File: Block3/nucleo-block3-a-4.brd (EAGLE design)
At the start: 100.3 x 80 mm, 91 parts, among them IC2 TL331, J4 MODJACK6P6C-MJ3245-66-0CONN_M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, J5 MODJACK6P6C-MJ3245-66-0CONN_M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, Q1 NPN-23, Q3 BSS84, Q4 BSS123, U1 TC4428ACOA, U2 TC4428ACOA, U3 TC4428ACOA

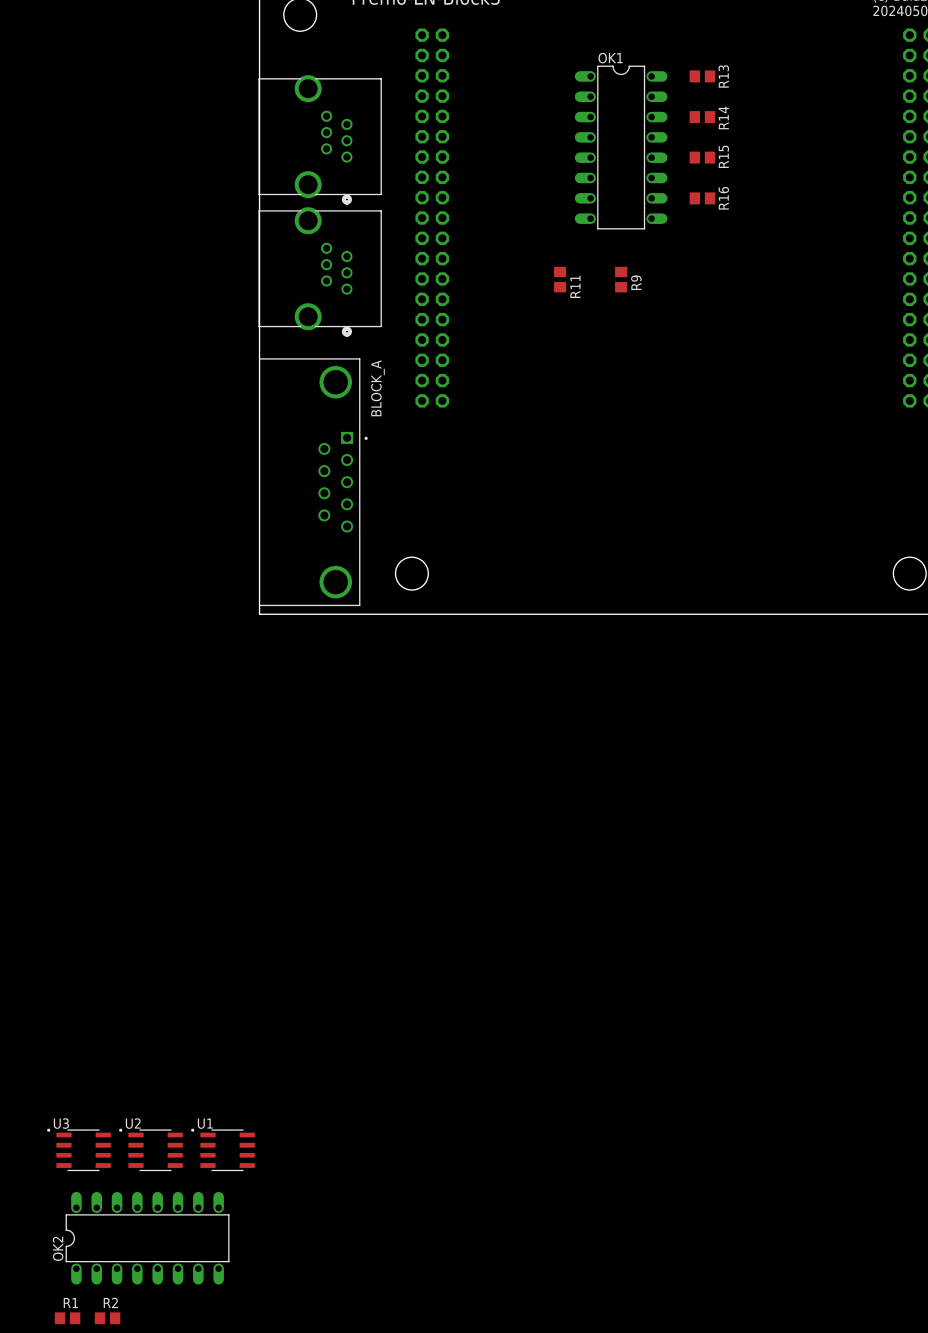
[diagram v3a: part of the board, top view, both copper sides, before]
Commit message: Arranges the optocouplers.
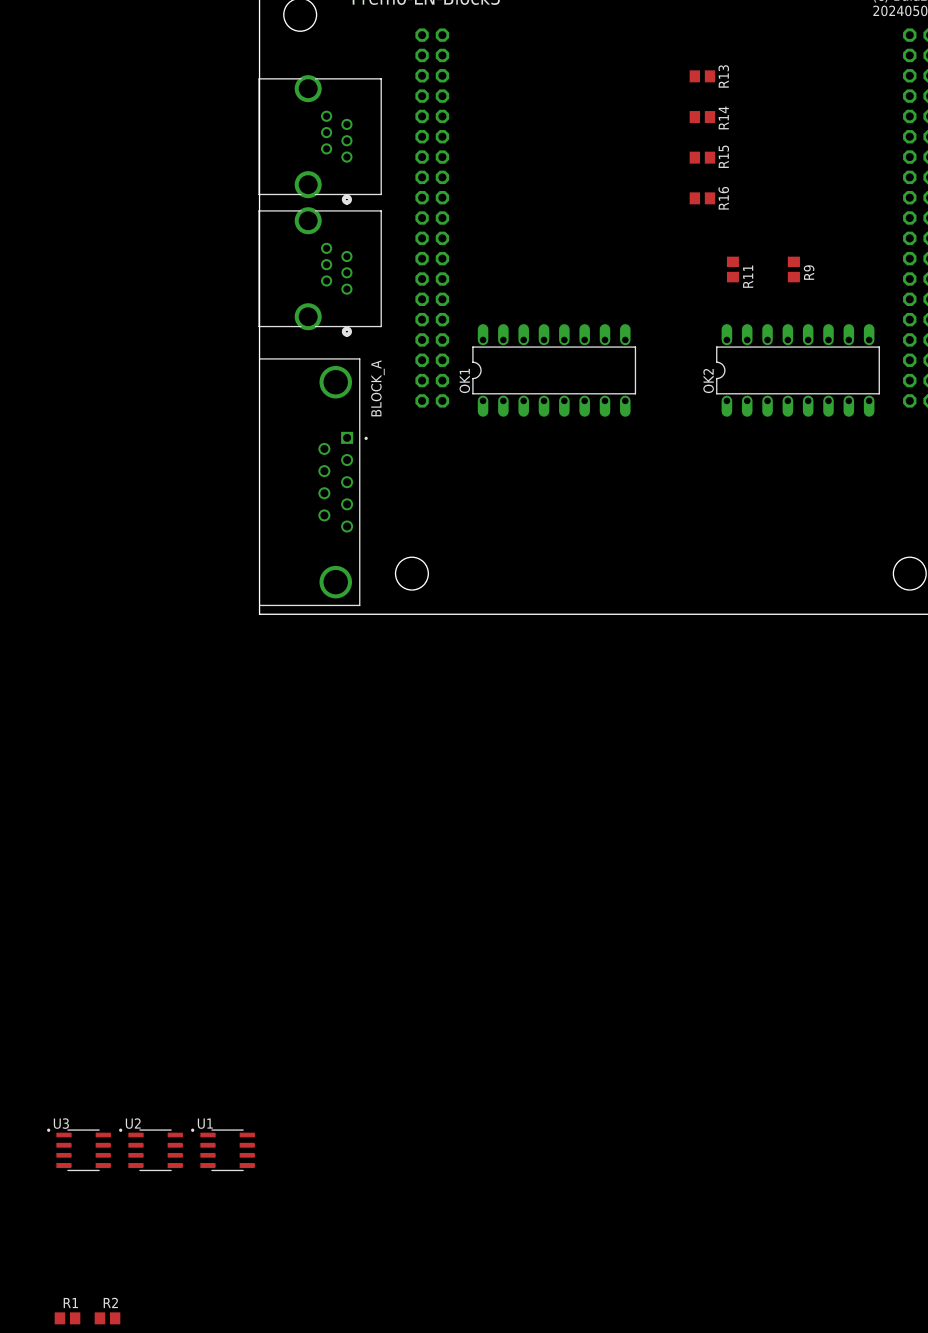
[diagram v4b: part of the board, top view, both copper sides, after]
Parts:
- moved OK2 135.6 mm to (67.3, 30.5)
- moved OK1 29.1 mm to (36.8, 30.5), turned to 0 degrees
- moved R11 21.6 mm to (59.2, 43.1)
- moved R9 21.6 mm to (66.8, 43.1)
